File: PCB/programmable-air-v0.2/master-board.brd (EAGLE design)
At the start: 101.7 x 50.9 mm, 20 parts, among them J1 POWER_JACKTOE

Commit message: Post Rube Goldberg. Working on PCB v0.2
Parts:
- removed J4: (no value), SparkFun-Connectors:1X08
- added D1, D2: (no value), SparkFun-LED:LED-0603
- added R3, R4: 4.7k, SparkFun-Resistors:0603
- added S1, S2: MOMENTARY-SWITCH-SPST-SMD-5.2MM, SparkFun-Switches:TACTILE_SWITCH_SMD_5.2MM
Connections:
- removed net N$29: ARDUINO_NANO1.4, J5.4
- new net GGRID: D1.A, U$1.P$1, U$3.P$1
- new net N$12: D1.C, R3.1
- new net N$17: D2.C, R4.1
- net GND: no longer J4.8
- net N$10: now also ARDUINO_NANO1.30; no longer ARDUINO_NANO1.7
- net N$11: now also ARDUINO_NANO1.5, J5.4; no longer ARDUINO_NANO1.8, J4.6
- net N$13: no longer J4.5
- net N$14: now also ARDUINO_NANO1.4; no longer ARDUINO_NANO1.10
- net N$15: now also ARDUINO_NANO1.20; no longer ARDUINO_NANO1.11
- net N$16: now also ARDUINO_NANO1.9; no longer ARDUINO_NANO1.20, J4.2
- net N$18: now also ARDUINO_NANO1.8; no longer ARDUINO_NANO1.30, J4.4
- net N$20: no longer J4.7
- net N$27: now also ARDUINO_NANO1.7; no longer ARDUINO_NANO1.6
- net N$28: now also ARDUINO_NANO1.6; no longer ARDUINO_NANO1.5
- net N$5: now also R3.2
- net N$6: now also R4.2
- net N$8: no longer J4.3
- net VIN: now also D2.A; no longer J4.1, U$1.P$1, U$3.P$1
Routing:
- net N$11: track 85.0 -> 0.00 mm
- net N$16: track 70.9 -> 0.00 mm
- net N$18: track 44.4 -> 0.00 mm
- net N$29: track 39.5 -> 0.00 mm
- net N$28: track 39.5 -> 30.6 mm
- net N$27: track 39.5 -> 30.6 mm
- net N$8: track 66.8 -> 60.5 mm
- net VIN: track 241.8 -> 235.6 mm
- net N$20: track 180.1 -> 175.0 mm
- net GND: track 23.8 -> 21.2 mm, vias 8 -> 7
- net N$15: track 44.6 -> 43.2 mm
- net N$10: track 10.6 -> 9.75 mm
- net N$13: track 162.7 -> 161.9 mm
- net N$14: track 67.7 -> 67.0 mm

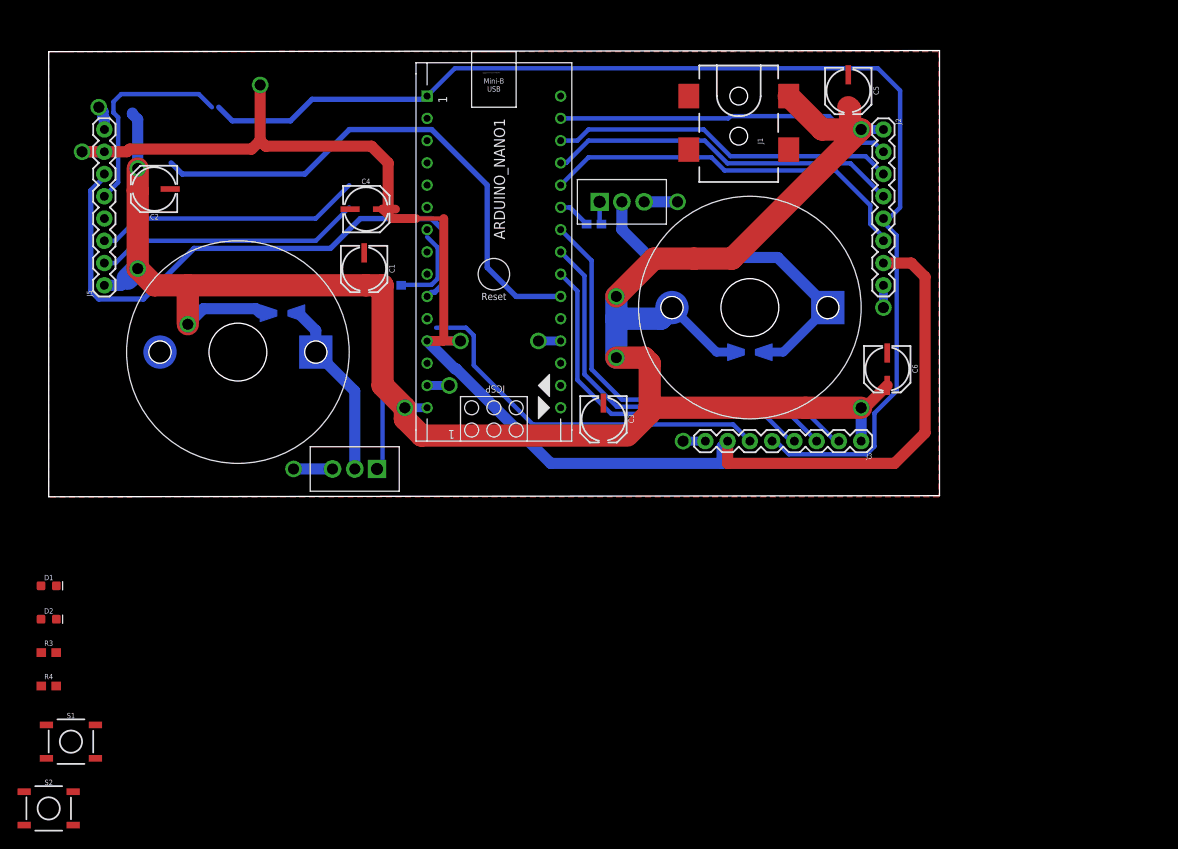
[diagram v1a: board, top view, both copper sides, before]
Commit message: Master PCB v0.2 schematic and positioning complee. Going to start routing
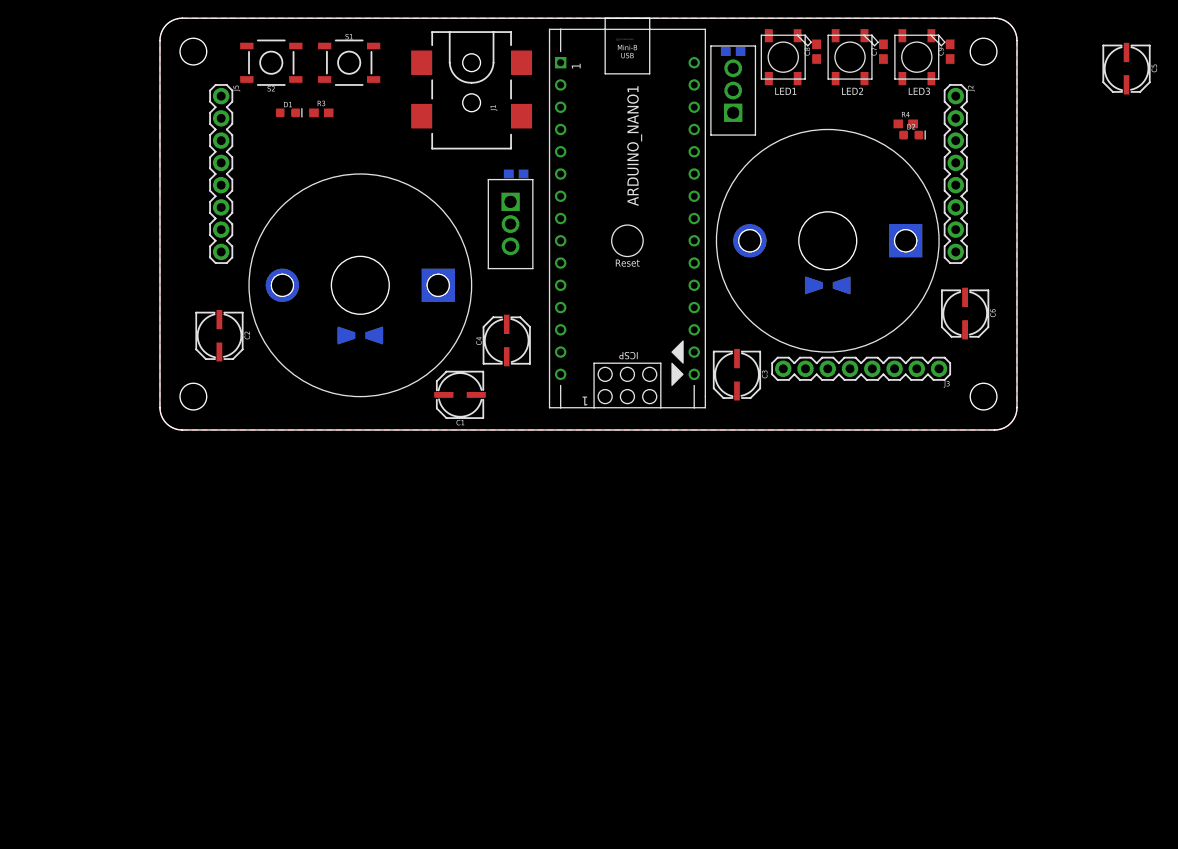
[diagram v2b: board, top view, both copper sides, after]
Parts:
- added C7, C8, C9: 0.1uF, SparkFun-Capacitors:0603
- added LED1, LED2, LED3: WS2812B5050, adafruit:WS2812B
- moved R4 116.9 mm to (97.8, 42.5)
- moved D2 112.9 mm to (98.4, 41.3)
- moved S2 88.8 mm to (25.4, 49.5), turned to 180 degrees
- moved S1 83.7 mm to (34.3, 49.5)
- moved R3 69.0 mm to (31.1, 43.8)
- moved D1 60.5 mm to (27.3, 43.8)
- moved U$6 33.1 mm to (52.7, 31.1), turned to 270 degrees
- moved C5 31.9 mm to (123.2, 48.9)
- moved J1 30.7 mm to (48.3, 49.5)
- moved J5 25.4 mm to (19.7, 45.7), turned to 270 degrees
- moved R2 25.3 mm to (78.1, 50.8)
- moved C4 22.0 mm to (52.1, 17.8), turned to 90 degrees
- moved R1 18.9 mm to (53.3, 36.8)
- moved C2 18.2 mm to (19.7, 18.4), turned to 270 degrees
- moved C1 18.2 mm to (47.0, 11.4), turned to 180 degrees
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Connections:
- removed net GGRID: D1.A, U$1.P$1, U$3.P$1
- removed net N$16: ARDUINO_NANO1.9
- removed net N$18: ARDUINO_NANO1.8
- removed net N$20: ARDUINO_NANO1.12, C4.+, J2.7, J3.7, J5.7
- new net N$19: ARDUINO_NANO1.20, S1.1
- new net N$21: LED2.2-DOUT, LED3.4-DIN
- new net N$26: LED1.2-DOUT, LED2.4-DIN
- new net N$29: ARDUINO_NANO1.21, S2.1
- new net VCC: ARDUINO_NANO1.12, C4.+, C7.1, C8.1, C9.1, J2.7, J3.7, J5.7, LED1.1-VDD, LED2.1-VDD, LED3.1-VDD
- net GND: now also C7.2, C8.2, C9.2, LED1.3-GND, LED2.3-GND, LED3.3-GND, S1.3, S2.3
- net N$1: now also ARDUINO_NANO1.29; no longer ARDUINO_NANO1.25
- net N$10: now also ARDUINO_NANO1.28; no longer ARDUINO_NANO1.30
- net N$15: now also ARDUINO_NANO1.9; no longer ARDUINO_NANO1.20
- net N$22: now also ARDUINO_NANO1.24; no longer ARDUINO_NANO1.26
- net N$23: now also ARDUINO_NANO1.25; no longer ARDUINO_NANO1.27
- net N$24: now also ARDUINO_NANO1.26; no longer ARDUINO_NANO1.28
- net N$25: now also ARDUINO_NANO1.27; no longer ARDUINO_NANO1.29
- net N$3: now also ARDUINO_NANO1.23, J3.2; no longer ARDUINO_NANO1.22, J3.4
- net N$4: now also ARDUINO_NANO1.22; no longer ARDUINO_NANO1.23
- net N$8: now also ARDUINO_NANO1.30, LED1.4-DIN; no longer ARDUINO_NANO1.21
- net N$9: now also ARDUINO_NANO1.8, J3.4; no longer ARDUINO_NANO1.24, J3.2
- net VIN: now also D1.A, U$1.P$1, U$3.P$1
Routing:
- net VIN: track 235.6 -> 0.00 mm, vias 8 -> 0
- net N$20: track 175.0 -> 0.00 mm, vias 3 -> 0
- net N$13: track 161.9 -> 0.00 mm
- net N$14: track 67.0 -> 0.00 mm
- net N$8: track 60.5 -> 0.00 mm
- net N$9: track 49.0 -> 0.00 mm
- net N$4: track 44.7 -> 0.00 mm
- net N$22: track 43.6 -> 0.00 mm
- net N$15: track 43.2 -> 0.00 mm
- net N$3: track 40.5 -> 0.00 mm
- net N$23: track 40.5 -> 0.00 mm
- net N$6: track 39.5 -> 0.00 mm
- net N$24: track 39.5 -> 0.00 mm
- net N$25: track 38.6 -> 0.00 mm
- net N$28: track 30.6 -> 0.00 mm
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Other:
- board size 101.7 x 50.9 mm -> 97.8 x 47 mm

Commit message: Master PCB v0.2 routing complete
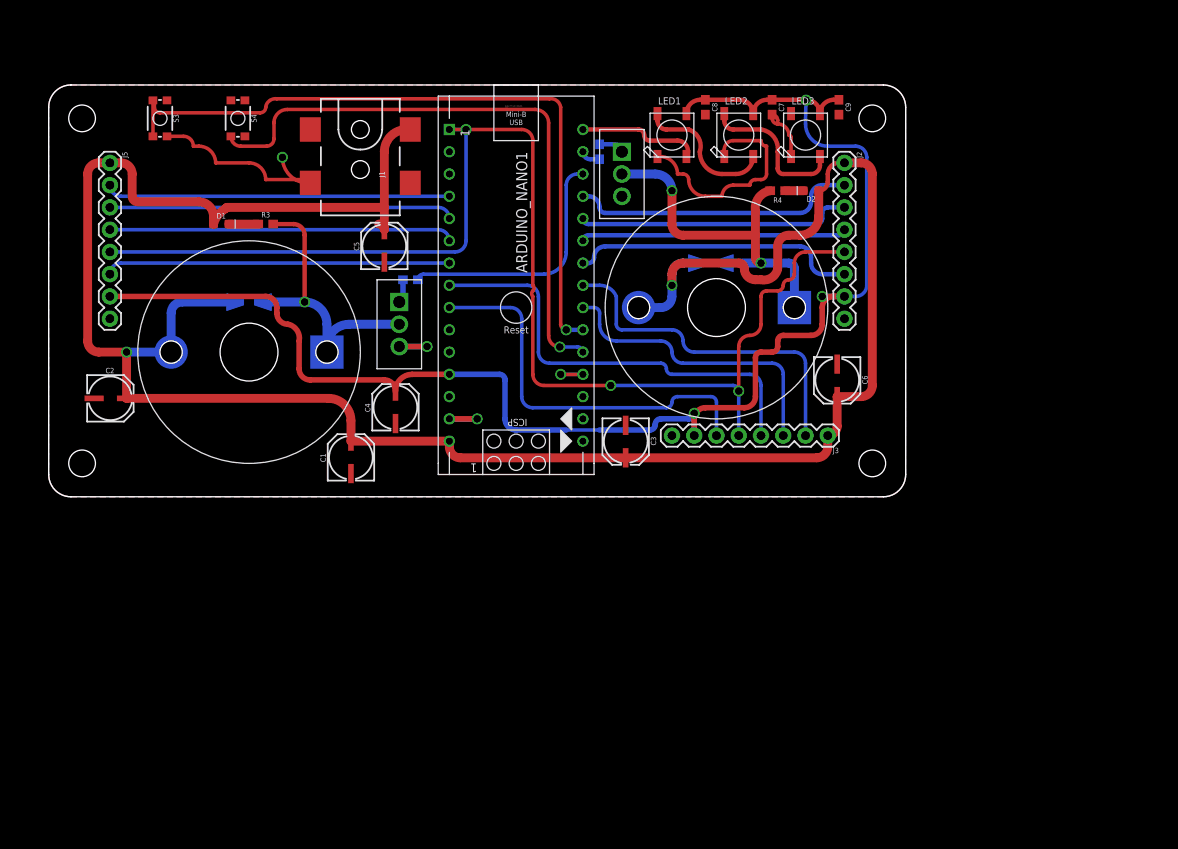
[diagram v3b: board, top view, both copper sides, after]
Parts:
- removed S1, S2: MOMENTARY-SWITCH-SPST-SMD-5.2MM, SparkFun-Switches:TACTILE_SWITCH_SMD_5.2MM
- added S3, S4: (no value), SparkFun-Switches:TACTILE_SWITCH_SMD_4.6X2.8MM
- moved C5 87.5 mm to (38.1, 28.6), turned to 90 degrees
- moved R2 19.1 mm to (62.9, 39.4), turned to 90 degrees
- moved U$6 17.1 mm to (40.0, 19.7)
- moved R1 17.1 mm to (41.3, 24.8)
- moved R4 16.5 mm to (83.2, 34.9), turned to 180 degrees
- moved C6 16.5 mm to (90.2, 13.3)
- moved U$5 15.9 mm to (65.4, 36.8), turned to 270 degrees
- moved LED2 15.5 mm to (78.7, 41.3), turned to 90 degrees
- moved LED3 15.5 mm to (86.4, 41.3), turned to 90 degrees
- moved LED1 15.5 mm to (71.1, 41.3), turned to 90 degrees
- moved ARDUINO_NANO1 14.8 mm to (53.3, 21.6)
- moved C4 14.8 mm to (39.4, 10.2)
- moved U$1 14.8 mm to (22.9, 16.5)
- moved U$2 14.8 mm to (76.2, 21.6)
- moved D1 14.8 mm to (19.7, 31.1)
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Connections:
- removed net N$19: ARDUINO_NANO1.20, S1.1
- removed net N$27: ARDUINO_NANO1.7, J5.2
- removed net N$28: ARDUINO_NANO1.6, J5.3
- new net N$16: ARDUINO_NANO1.4, J5.2
- new net N$18: ARDUINO_NANO1.6, J5.4
- new net N$20: ARDUINO_NANO1.20, S4.1, S4.2
- net GND: now also S3.3, S3.4, S4.3, S4.4; no longer S1.3, S2.3
- net N$11: now also J5.3; no longer J5.4
- net N$14: now also ARDUINO_NANO1.7; no longer ARDUINO_NANO1.4
- net N$29: now also S3.1, S3.2; no longer S2.1
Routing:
- net VIN: track 0.00 -> 265.5 mm, vias 0 -> 2
- net VCC: track 0.00 -> 166.6 mm, vias 0 -> 3
- net N$13: track 0.00 -> 146.1 mm, vias 0 -> 3
- net N$29: track 0.00 -> 80.0 mm, vias 0 -> 1
- net GND: track 0.00 -> 72.8 mm, vias 0 -> 4
- net N$20: track 0.00 -> 69.2 mm, vias 0 -> 1
- net N$9: track 0.00 -> 49.7 mm
- net N$15: track 0.00 -> 45.0 mm
- net N$6: track 0.00 -> 41.8 mm, vias 0 -> 2
- net N$11: track 0.00 -> 39.3 mm
- net N$18: track 0.00 -> 39.3 mm
- net N$16: track 0.00 -> 39.3 mm
- net N$14: track 0.00 -> 39.3 mm
- net N$3: track 0.00 -> 39.1 mm
- net N$4: track 0.00 -> 33.7 mm
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- added copper zone on layer 16, net GND

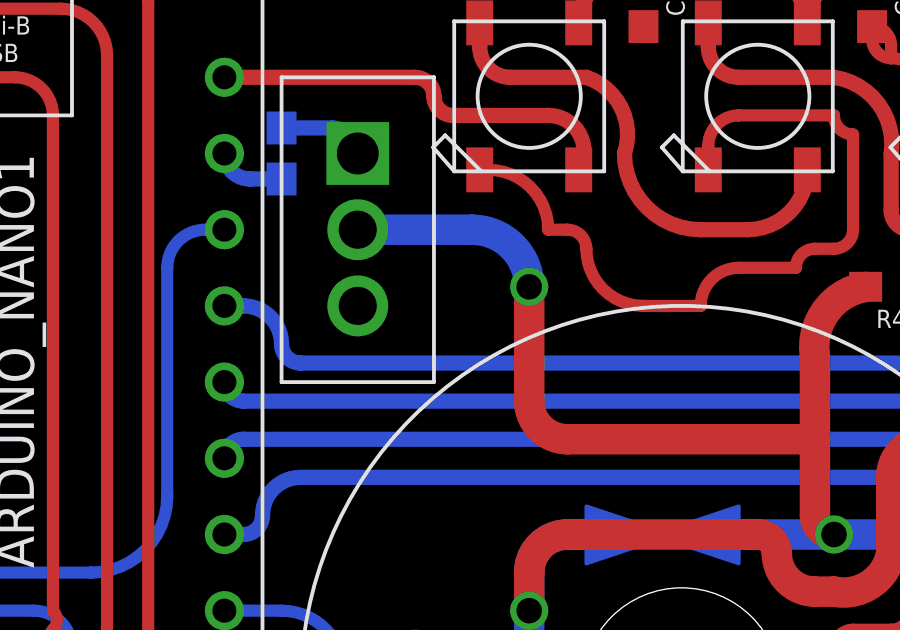
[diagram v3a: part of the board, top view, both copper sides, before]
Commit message: PCB v0.2 slave board ready
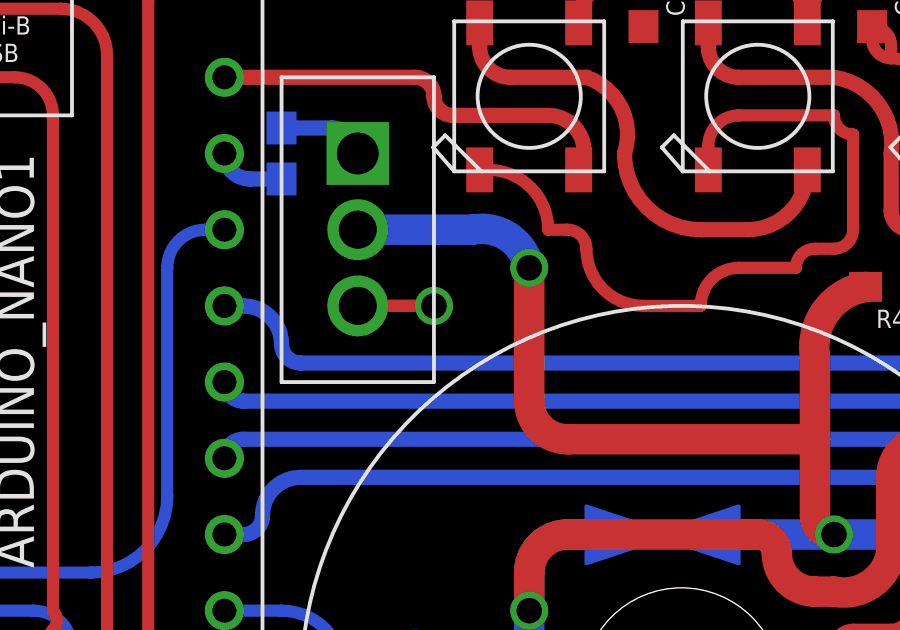
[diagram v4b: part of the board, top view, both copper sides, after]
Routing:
- net GND: track 72.8 -> 77.8 mm, vias 4 -> 5
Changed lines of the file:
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@@
 <wire x1="80.645" y1="27.305" x2="80.645" y2="29.845" width="1.016" layer="1"/>
 <wire x1="65.405" y1="36.83" x2="69.215" y2="36.83" width="1.016" layer="16"/>
-<wire x1="69.215" y1="36.83" x2="71.12" y2="34.925" width="1.016" layer="16" curve="-90"/>
-<via x="71.12" y="34.925" extent="1-16" drill="0.85"/>
+<wire x1="69.215" y1="36.83" x2="71.12" y2="35.56" width="1.016" layer="16" curve="-90"/>
+<via x="71.12" y="35.56" extent="1-16" drill="0.85"/>
 <wire x1="71.12" y1="31.115" x2="72.39" y2="29.845" width="1.016" layer="1" curve="90"/>
 <wire x1="72.39" y1="29.845" x2="80.645" y2="29.845" width="1.016" layer="1"/>
-<wire x1="71.12" y1="34.925" x2="71.12" y2="31.115" width="1.016" layer="1"/>
+<wire x1="71.12" y1="35.56" x2="71.12" y2="31.115" width="1.016" layer="1"/>
 <wire x1="80.645" y1="29.845" x2="80.645" y2="32.6" width="1.016" layer="1"/>
 <wire x1="80.645" y1="32.6" x2="82.335" y2="34.925" width="1.016" layer="1" curve="-90"/>
@@
 <wire x1="82.55" y1="43.6" x2="82.55" y2="43.18" width="0.4064" layer="1"/>
 <wire x1="82.55" y1="43.18" x2="83.185" y2="42.545" width="0.4064" layer="1" curve="90"/>
+<wire x1="65.405" y1="34.29" x2="67.945" y2="34.29" width="0.4064" layer="1"/>
+<via x="67.945" y="34.29" extent="1-16" drill="0.85"/>
+<wire x1="67.945" y1="34.29" x2="65.405" y2="34.29" width="0.4064" layer="16"/>
+<wire x1="13.5" y1="41.13" x2="13.5" y2="45.23" width="0" layer="19" extent="1-1"/>
 <wire x1="22.39" y1="45.23" x2="22.39" y2="41.13" width="0" layer="19" extent="1-1"/>
-<wire x1="13.5" y1="45.23" x2="13.5" y2="41.13" width="0" layer="19" extent="1-1"/>
 </signal>
 <signal name="N$13">

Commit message: PCB v0.2 cosmetic changes
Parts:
- moved R3 6.75 mm to (19.7, 35.6)
- moved D1 6.75 mm to (14.6, 35.6)
- moved U$3 6.35 mm to (22.9, 15.9)
- moved C2 5.85 mm to (11.4, 7.62), turned to 90 degrees
- moved U$1 5.08 mm to (22.9, 21.6)
- moved C1 3.70 mm to (32.4, 7.62)
- moved C4 2.62 mm to (40.0, 7.62)
- moved C3 1.27 mm to (66.0, 7.62)
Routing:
- net VIN: track 265.5 -> 290.2 mm, vias 2 -> 4
- net GND: track 77.8 -> 59.3 mm
- net N$5: track 32.3 -> 46.9 mm, vias 1 -> 3
- net VCC: track 166.6 -> 171.6 mm
- net N$11: track 39.3 -> 40.8 mm
- net N$18: track 39.3 -> 40.3 mm
- net N$16: track 39.3 -> 40.3 mm
- net N$14: track 39.3 -> 40.3 mm
- net N$13: track 146.1 -> 147.1 mm
